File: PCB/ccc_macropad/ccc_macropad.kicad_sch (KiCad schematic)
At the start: 18 parts, among them SW1 SW_Push, SW2 SW_Push, SW3 OS/Left_Right-hand_Switch, SW4 SW_Push, SW5 SW_Push, U1 XIAO-RP2040-DIP

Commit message: feat: update BOM and OS_switch
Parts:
- SW1, SW2, SW4, SW5: footprint Button_Switch_Keyboard:SW_Cherry_MX_1.00u_PCB -> Key_Switches:Kailh_socket_MX_PG1350_optional
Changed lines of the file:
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@@
 			)
 		)
-		(property "Footprint" "Button_Switch_Keyboard:SW_Cherry_MX_1.00u_PCB"
+		(property "Footprint" "Key_Switches:Kailh_socket_MX_PG1350_optional"
 			(at 161.29 107.95 0)
 			(effects
@@
 			)
 		)
-		(property "Footprint" "Button_Switch_Keyboard:SW_Cherry_MX_1.00u_PCB"
+		(property "Footprint" "Key_Switches:Kailh_socket_MX_PG1350_optional"
 			(at 194.31 100.33 0)
 			(effects
@@
 			)
 		)
-		(property "Footprint" "Button_Switch_Keyboard:SW_Cherry_MX_1.00u_PCB"
+		(property "Footprint" "Key_Switches:Kailh_socket_MX_PG1350_optional"
 			(at 194.31 114.3 0)
 			(effects
@@
 			)
 		)
-		(property "Footprint" "Button_Switch_Keyboard:SW_Cherry_MX_1.00u_PCB"
+		(property "Footprint" "Key_Switches:Kailh_socket_MX_PG1350_optional"
 			(at 161.29 121.92 0)
 			(effects

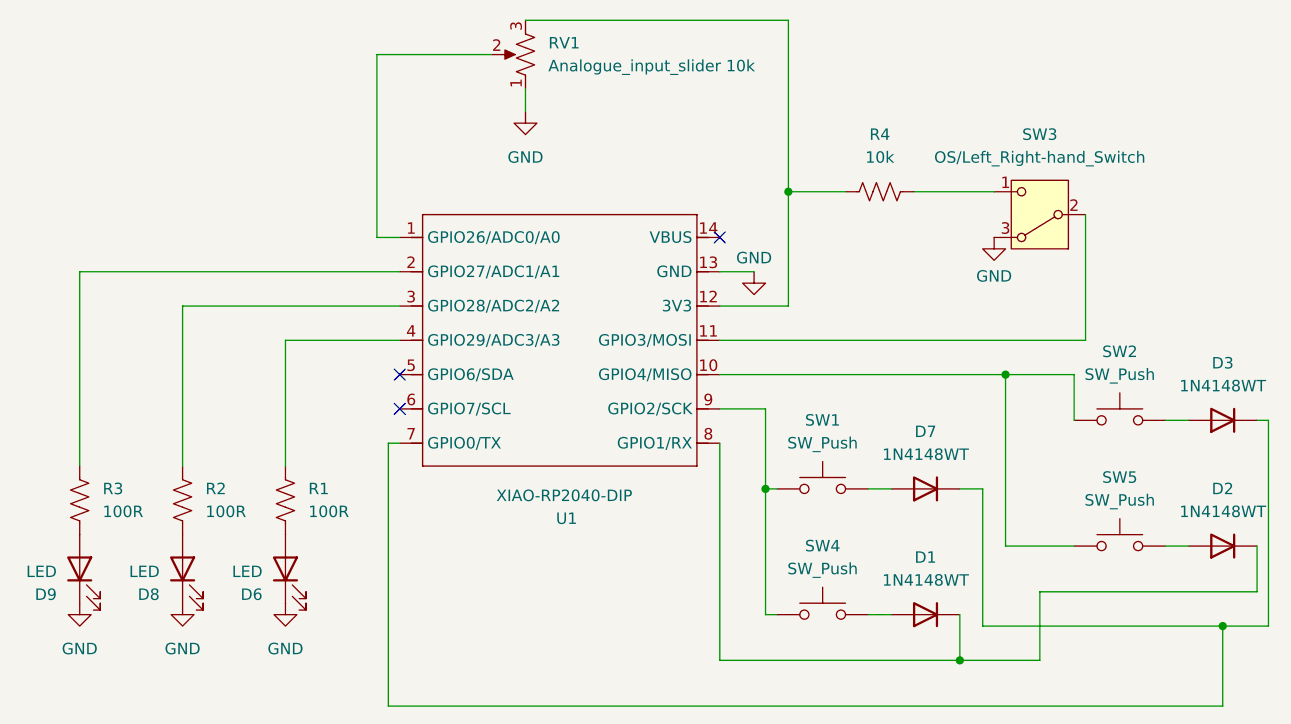
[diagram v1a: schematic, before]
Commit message: feat: create and include all footprint. import all components in PCB
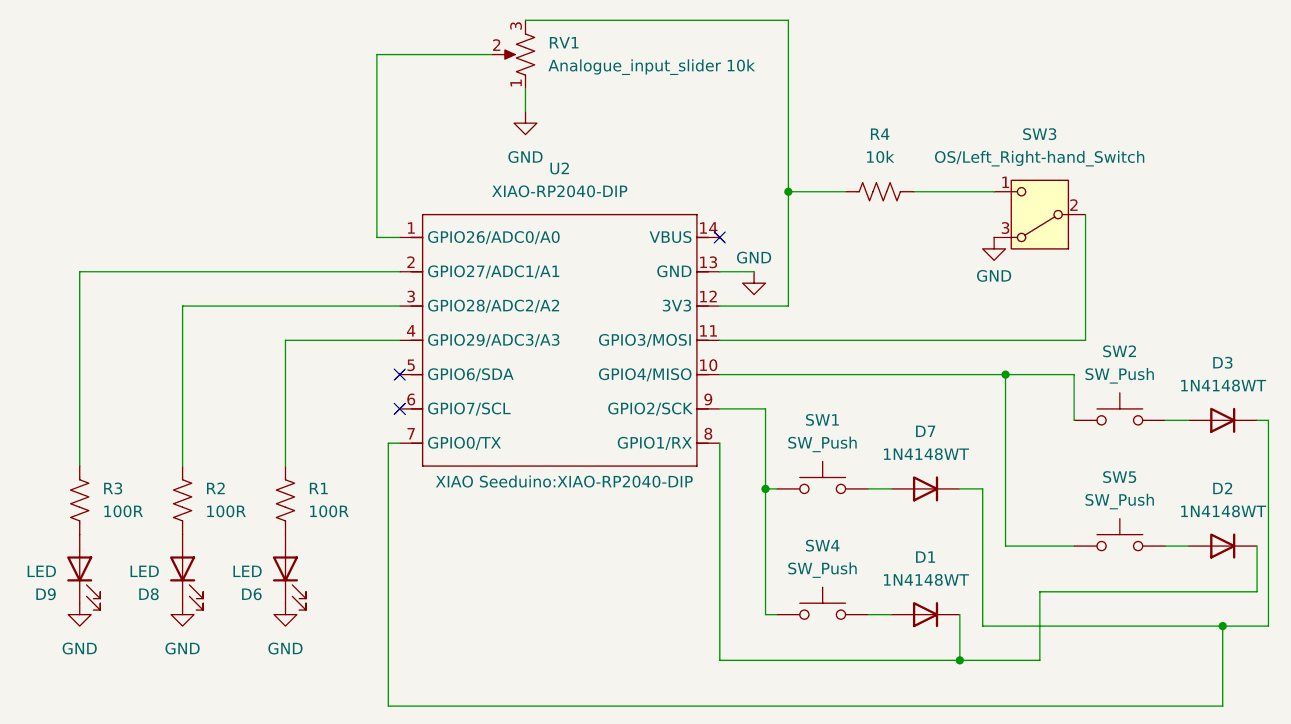
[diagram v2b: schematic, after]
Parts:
- removed U1: XIAO-RP2040-DIP, XIAO Seeduino:XIAO-RP2040-DIP, symbol Seeed XIAO:XIAO-RP2040-DIP
- added U2: XIAO-RP2040-DIP, XIAO Seeduino:XIAO-RP2040-DIP, symbol Seeed XIAO:XIAO-RP2040-DIP
- D1, D2, D3, D7: footprint Diode_SMD:D_SOD-523 -> Key_Switches:D_DO-35_SOD27_P5.08mm_Horizontal
- R1, R2, R3, R4: footprint Resistor_THT:R_Axial_DIN0207_L6.3mm_D2.5mm_P10.16mm_Horizontal -> Resistor_THT:R_Axial_DIN0204_L3.6mm_D1.6mm_P5.08mm_Horizontal
- RV1: footprint Potentiometer_THT:Potentiometer_Bourns_PTA4543_Single_Slide -> CustomFootprints:Potentiometer_slide_75mm_range_60mm_2_sets
- SW3: footprint Button_Switch_SMD:Nidec_Copal_CAS-120A -> CustomFootprints:SPDT_3pin_2_pos_1P2T_tht_2.54mm_switch_sk12d07
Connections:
- net GND: now also U2.13 (GND)
- net at R4.2, RV1.3: now also U2.12 (3V3)
- net at SW1.1, SW4.1: now also U2.9 (GPIO2/SCK)
- net at SW2.1, SW5.1: now also U2.10 (GPIO4/MISO)
- net at D1.1 (K), D2.1 (K): now also U2.8 (GPIO1/RX)
- net at D3.1 (K), D7.1 (K): now also U2.7 (GPIO0/TX)
- net at R1.2: now also U2.4 (GPIO29/ADC3/A3)
- net at RV1.2: now also U2.1 (GPIO26/ADC0/A0)
- net at SW3.2 (B): now also U2.11 (GPIO3/MOSI)
- net at R3.2: now also U2.2 (GPIO27/ADC1/A1)
- net at R2.2: now also U2.3 (GPIO28/ADC2/A2)
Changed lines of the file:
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@@
 			)
 		)
-		(property "Footprint" "Resistor_THT:R_Axial_DIN0207_L6.3mm_D2.5mm_P10.16mm_Horizontal"
+		(property "Footprint" "Resistor_THT:R_Axial_DIN0204_L3.6mm_D1.6mm_P5.08mm_Horizontal"
 			(at 167.386 81.026 90)
 			(effects
@@
 	)
 	(symbol
+		(lib_id "Seeed XIAO:XIAO-RP2040-DIP")
+		(at 118.11 80.01 0)
+		(unit 1)
+		(exclude_from_sim no)
+		(in_bom yes)
+		(on_board yes)
+		(dnp no)
+		(fields_autoplaced yes)
+		(property "Reference" "U2"
+			(at 132.08 77.47 0)
+			(effects
+				(font
+					(size 1.27 1.27)
+				)
+			)
+		)
+		(property "Value" "XIAO-RP2040-DIP"
+			(at 132.08 80.01 0)
+			(effects
+				(font
+					(size 1.27 1.27)
+				)
+			)
+		)
+		(property "Footprint" "XIAO Seeduino:XIAO-RP2040-DIP"
+			(at 132.588 112.268 0)
+			(effects
+				(font
+					(size 1.27 1.27)
+				)
+			)
+		)
+		(property "Datasheet" ""
+			(at 118.11 80.01 0)
+			(effects
+				(font
+					(size 1.27 1.27)
+				)
+				(hide yes)
+			)
+		)
+		(property "Description" ""
+			(at 118.11 80.01 0)
+			(effects
+				(font
+					(size 1.27 1.27)
+				)
+				(hide yes)
+			)
+		)
+		(pin "11"
+		)
+		(pin "7"
+		)
+		(pin "9"
+		)
+		(pin "10"
+		)
+		(pin "12"
+		)
+		(pin "8"
+		)
+		(pin "6"
+		)
+		(pin "5"
+		)
+		(pin "3"
+		)
+		(pin "2"
+		)
+		(pin "1"
+		)
+		(pin "13"
+		)
+		(pin "14"
+		)
+		(pin "4"
+		)
+		(instances
+			(project ""
+				(path "/30b7c58f-86a9-47fb-ba55-c2e4c0b4123f"
+					(reference "U2")
+					(unit 1)
+				)
+			)
+		)
+	)
+	(symbol
 		(lib_id "Switch:SW_Push")
 		(at 194.31 105.41 0)
@@
 			)
 		)
-		(property "Footprint" "Diode_SMD:D_SOD-523"
+		(property "Footprint" "Key_Switches:D_DO-35_SOD27_P5.08mm_Horizontal"
 			(at 172.72 122.555 0)
 			(effects
@@
 			)
 		)
-		(property "Footprint" "Diode_SMD:D_SOD-523"
+		(property "Footprint" "Key_Switches:D_DO-35_SOD27_P5.08mm_Horizontal"
 			(at 172.72 108.585 0)
 			(effects
@@
 			)
 		)
-		(property "Footprint" "Resistor_THT:R_Axial_DIN0207_L6.3mm_D2.5mm_P10.16mm_Horizontal"
+		(property "Footprint" "Resistor_THT:R_Axial_DIN0204_L3.6mm_D1.6mm_P5.08mm_Horizontal"
 			(at 100.584 114.046 90)
 			(effects
@@
 	)
 	(symbol
-		(lib_id "Seeed XIAO:XIAO-RP2040-DIP")
-		(at 118.11 80.01 0)
-		(unit 1)
-		(exclude_from_sim no)
-		(in_bom yes)
-		(on_board yes)
-		(dnp no)
-		(property "Reference" "U1"
-			(at 132.842 116.332 0)
-			(effects
-				(font
-					(size 1.27 1.27)
-				)
-			)
-		)
-		(property "Value" "XIAO-RP2040-DIP"
-			(at 132.588 113.792 0)
-			(effects
-				(font
-					(size 1.27 1.27)
-				)
-			)
-		)
-		(property "Footprint" "XIAO Seeduino:XIAO-RP2040-DIP"
-			(at 132.588 112.268 0)
-			(effects
-				(font
-					(size 1.27 1.27)
-				)
-				(hide yes)
-			)
-		)
-		(property "Datasheet" ""
-			(at 118.11 80.01 0)
-			(effects
-				(font
-					(size 1.27 1.27)
-				)
-				(hide yes)
-			)
-		)
-		(property "Description" ""
-			(at 118.11 80.01 0)
-			(effects
-				(font
-					(size 1.27 1.27)
-				)
-				(hide yes)
-			)
-		)
-		(pin "1"
-		)
-		(pin "3"
-		)
-		(pin "4"
-		)
-		(pin "14"
-		)
-		(pin "13"
-		)
-		(pin "5"
-		)
-		(pin "6"
-		)
-		(pin "7"
-		)
-		(pin "10"
-		)
-		(pin "11"
-		)
-		(pin "12"
-		)
-		(pin "9"
-		)
-		(pin "2"
-		)
-		(pin "8"
-		)
-		(instances
-			(project ""
-				(path "/30b7c58f-86a9-47fb-ba55-c2e4c0b4123f"
-					(reference "U1")
-					(unit 1)
-				)
-			)
-		)
-	)
-	(symbol
 		(lib_id "Device:R_Potentiometer_US")
 		(at 128.27 64.77 180)
@@
 			)
 		)
-		(property "Footprint" "Potentiometer_THT:Potentiometer_Bourns_PTA4543_Single_Slide"
+		(property "Footprint" "CustomFootprints:Potentiometer_slide_75mm_range_60mm_2_sets"
 			(at 128.27 64.77 0)
 			(effects
@@
 			)
 		)
-		(property "Footprint" "Button_Switch_SMD:Nidec_Copal_CAS-120A"
+		(property "Footprint" "CustomFootprints:SPDT_3pin_2_pos_1P2T_tht_2.54mm_switch_sk12d07"
 			(at 185.42 72.39 0)
 			(effects
@@
 			)
 		)
-		(property "Footprint" "Diode_SMD:D_SOD-523"
+		(property "Footprint" "Key_Switches:D_DO-35_SOD27_P5.08mm_Horizontal"
 			(at 205.74 114.935 0)
 			(effects
@@
 			)
 		)
-		(property "Footprint" "Resistor_THT:R_Axial_DIN0207_L6.3mm_D2.5mm_P10.16mm_Horizontal"
+		(property "Footprint" "Resistor_THT:R_Axial_DIN0204_L3.6mm_D1.6mm_P5.08mm_Horizontal"
 			(at 89.154 114.046 90)
 			(effects
@@
 			)
 		)
-		(property "Footprint" "Diode_SMD:D_SOD-523"
+		(property "Footprint" "Key_Switches:D_DO-35_SOD27_P5.08mm_Horizontal"
 			(at 205.74 100.965 0)
 			(effects
@@
 			)
 		)
-		(property "Footprint" "Resistor_THT:R_Axial_DIN0207_L6.3mm_D2.5mm_P10.16mm_Horizontal"
+		(property "Footprint" "Resistor_THT:R_Axial_DIN0204_L3.6mm_D1.6mm_P5.08mm_Horizontal"
 			(at 77.724 114.046 90)
 			(effects
